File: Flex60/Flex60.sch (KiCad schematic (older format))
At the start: 112 parts

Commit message: Layout Diodes + add flex cuts
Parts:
- removed D31: BAV70, Custom_Footprints:SOT-23_Annotated, symbol Diode:BAV70
- renumbered D32 to D31, D33 to D32
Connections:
- net at K_0.2: now also D1.2 (A); no longer D1.1 (A)
- net at K_1.2: now also D1.1 (A); no longer D1.2 (A)
- net at K_100.2: now also D8.2 (A); no longer D8.1 (A)
- net at K_101.2: now also D8.1 (A); no longer D8.2 (A)
- net at K_200.2, K_200A1.2: now also D15.2 (A); no longer D15.1 (A)
- net at K_201.2: now also D15.1 (A); no longer D15.2 (A)
- net at K_300.2: now also D22.2 (A); no longer D22.1 (A)
- net at K_301.2: now also D22.1 (A); no longer D22.2 (A)
- net at K_400.2, K_400A1.2: now also D29.2 (A); no longer D29.1 (A)
- net at K_401.2, K_401A1.2: now also D29.1 (A); no longer D29.2 (A)
- net at K_2.2: now also D2.2 (A); no longer D2.1 (A)
- net at K_3.2: now also D2.1 (A); no longer D2.2 (A)
- net at K_102.2: now also D9.2 (A); no longer D9.1 (A)
- net at K_103.2: now also D9.1 (A); no longer D9.2 (A)
- net at K_202.2: now also D16.2 (A); no longer D16.1 (A)
- net at K_203.2: now also D16.1 (A); no longer D16.2 (A)
- net at K_302.2: now also D23.2 (A); no longer D23.1 (A)
- net at K_303.2: now also D23.1 (A); no longer D23.2 (A)
- net at K_402.2, K_402A1.2: now also D30.2 (A); no longer D30.1 (A)
- net at K_4.2: now also D3.2 (A); no longer D3.1 (A)
- net at K_5.2: now also D3.1 (A); no longer D3.2 (A)
- net at K_104.2: now also D10.2 (A); no longer D10.1 (A)
- net at K_105.2: now also D10.1 (A); no longer D10.2 (A)
- net at K_204.2: now also D17.2 (A); no longer D17.1 (A)
- net at K_205.2: now also D17.1 (A); no longer D17.2 (A)
- net at K_304.2: now also D24.2 (A); no longer D24.1 (A)
- net at K_305.2: now also D24.1 (A); no longer D24.2 (A)
- net at K_6.2: now also D4.2 (A); no longer D4.1 (A)
- net at K_7.2: now also D4.1 (A); no longer D4.2 (A)
- net at K_106.2: now also D11.2 (A); no longer D11.1 (A)
- net at K_107.2: now also D11.1 (A); no longer D11.2 (A)
- net at K_206.2: now also D18.2 (A); no longer D18.1 (A)
- net at K_207.2: now also D18.1 (A); no longer D18.2 (A)
- net at K_306.2: now also D25.2 (A); no longer D25.1 (A)
- net at K_307.2: now also D25.1 (A); no longer D25.2 (A)
- net at K_406.2, K_406A1.2: now also D30.1 (A)
- net at K_8.2: now also D5.2 (A); no longer D5.1 (A)
- net at K_9.2: now also D5.1 (A); no longer D5.2 (A)
- net at K_108.2: now also D12.2 (A); no longer D12.1 (A)
- net at K_109.2: now also D12.1 (A); no longer D12.2 (A)
- net at K_208.2: now also D19.2 (A); no longer D19.1 (A)
- net at K_209.2: now also D19.1 (A); no longer D19.2 (A)
- net at K_308.2: now also D26.2 (A); no longer D26.1 (A)
- net at K_309.2: now also D26.1 (A); no longer D26.2 (A)
- net at K_408.2: now also D31.2 (A); no longer D31.1 (A)
- net at K_409.2, K_409A1.2: now also D31.1 (A); no longer D31.2 (A)
- net at K_10.2: now also D6.2 (A); no longer D6.1 (A)
- net at K_11.2: now also D6.1 (A); no longer D6.2 (A)
- net at K_110.2: now also D13.2 (A); no longer D13.1 (A)
- net at K_111.2: now also D13.1 (A); no longer D13.2 (A)
- net at K_210.2: now also D20.2 (A); no longer D20.1 (A)
- net at K_211.2: now also D20.1 (A); no longer D20.2 (A)
- net at K_310.2: now also D27.2 (A); no longer D27.1 (A)
- net at K_311.2, K_311A1.2: now also D27.1 (A); no longer D27.2 (A)
- net at K_410.2, K_410A1.2: now also D32.2 (A); no longer D32.1 (A)
- net at K_411.2, K_411A1.2: now also D32.1 (A); no longer D32.2 (A)
- net at K_12.2: now also D7.2 (A); no longer D7.1 (A)
- net at K_013A1.2, K_13.2: now also D7.1 (A); no longer D7.2 (A)
- net at K_112.2: now also D14.2 (A); no longer D14.1 (A)
- net at K_113.2: now also D14.1 (A); no longer D14.2 (A)
- net at K_212.2: now also D21.2 (A); no longer D21.1 (A)
- net at K_213.2: now also D21.1 (A); no longer D21.2 (A)
- no-connect marks 3 -> 1
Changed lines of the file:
@@
 F 3 "https://assets.nexperia.com/documents/data-sheet/BAV70_SER.pdf" H 1275 875 50  0001 C CNN
 	1    1275 875
-	1    0    0    -1
+	-1   0    0    -1
 $EndComp
 $Comp
@@
 F 3 "https://assets.nexperia.com/documents/data-sheet/BAV70_SER.pdf" H 1275 1450 50  0001 C CNN
 	1    1275 1450
-	1    0    0    -1
+	-1   0    0    -1
 $EndComp
 $Comp
@@
 F 3 "https://assets.nexperia.com/documents/data-sheet/BAV70_SER.pdf" H 1275 2025 50  0001 C CNN
 	1    1275 2025
-	1    0    0    -1
+	-1   0    0    -1
 $EndComp
 $Comp
@@
 F 3 "https://assets.nexperia.com/documents/data-sheet/BAV70_SER.pdf" H 1275 2600 50  0001 C CNN
 	1    1275 2600
-	1    0    0    -1
+	-1   0    0    -1
 $EndComp
 $Comp
@@
 F 3 "https://assets.nexperia.com/documents/data-sheet/BAV70_SER.pdf" H 1275 3175 50  0001 C CNN
 	1    1275 3175
-	1    0    0    -1
+	-1   0    0    -1
 $EndComp
 $Comp
@@
 F 3 "https://assets.nexperia.com/documents/data-sheet/BAV70_SER.pdf" H 2800 875 50  0001 C CNN
 	1    2800 875
-	1    0    0    -1
+	-1   0    0    -1
 $EndComp
 $Comp
@@
 F 3 "https://assets.nexperia.com/documents/data-sheet/BAV70_SER.pdf" H 2800 1450 50  0001 C CNN
 	1    2800 1450
-	1    0    0    -1
+	-1   0    0    -1
 $EndComp
 $Comp
@@
 F 3 "https://assets.nexperia.com/documents/data-sheet/BAV70_SER.pdf" H 2800 2025 50  0001 C CNN
 	1    2800 2025
-	1    0    0    -1
+	-1   0    0    -1
 $EndComp
 $Comp
@@
 F 3 "https://assets.nexperia.com/documents/data-sheet/BAV70_SER.pdf" H 2800 2600 50  0001 C CNN
 	1    2800 2600
-	1    0    0    -1
+	-1   0    0    -1
 $EndComp
 $Comp
@@
 F 3 "https://assets.nexperia.com/documents/data-sheet/BAV70_SER.pdf" H 2800 3175 50  0001 C CNN
 	1    2800 3175
-	1    0    0    -1
+	-1   0    0    -1
 $EndComp
 Wire Wire Line
@@
 F 3 "https://assets.nexperia.com/documents/data-sheet/BAV70_SER.pdf" H 4325 875 50  0001 C CNN
 	1    4325 875
-	1    0    0    -1
+	-1   0    0    -1
 $EndComp
 $Comp
@@
 F 3 "https://assets.nexperia.com/documents/data-sheet/BAV70_SER.pdf" H 4325 1450 50  0001 C CNN
 	1    4325 1450
-	1    0    0    -1
+	-1   0    0    -1
 $EndComp
 $Comp
@@
 F 3 "https://assets.nexperia.com/documents/data-sheet/BAV70_SER.pdf" H 4325 2025 50  0001 C CNN
 	1    4325 2025
-	1    0    0    -1
+	-1   0    0    -1
 $EndComp
 $Comp
@@
 F 3 "https://assets.nexperia.com/documents/data-sheet/BAV70_SER.pdf" H 4325 2600 50  0001 C CNN
 	1    4325 2600
-	1    0    0    -1
+	-1   0    0    -1
 $EndComp
 Wire Wire Line
@@
 F 3 "https://assets.nexperia.com/documents/data-sheet/BAV70_SER.pdf" H 5850 875 50  0001 C CNN
 	1    5850 875
-	1    0    0    -1
+	-1   0    0    -1
 $EndComp
 $Comp
@@
 F 3 "https://assets.nexperia.com/documents/data-sheet/BAV70_SER.pdf" H 5850 1450 50  0001 C CNN
 	1    5850 1450
-	1    0    0    -1
+	-1   0    0    -1
 $EndComp
 $Comp
@@
 F 3 "https://assets.nexperia.com/documents/data-sheet/BAV70_SER.pdf" H 5850 2025 50  0001 C CNN
 	1    5850 2025
-	1    0    0    -1
+	-1   0    0    -1
 $EndComp
 $Comp
@@
 F 3 "https://assets.nexperia.com/documents/data-sheet/BAV70_SER.pdf" H 5850 2600 50  0001 C CNN
 	1    5850 2600
-	1    0    0    -1
+	-1   0    0    -1
 $EndComp
 $Comp
@@
 	1    0    0    -1
 $EndComp
-$Comp
-L Diode:BAV70 D31
-U 1 1 5FD7F567
-P 5850 3175
-F 0 "D31" H 5850 3392 50  0000 C CNN
-F 1 "BAV70" H 5850 3301 50  0000 C CNN
-F 2 "Custom_Footprints:SOT-23_Annotated" H 5850 3175 50  0001 C CNN
-F 3 "https://assets.nexperia.com/documents/data-sheet/BAV70_SER.pdf" H 5850 3175 50  0001 C CNN
-	1    5850 3175
-	1    0    0    -1
-$EndComp
 Wire Wire Line
 	5850 2225 4325 2225
@@
 F 3 "https://assets.nexperia.com/documents/data-sheet/BAV70_SER.pdf" H 7375 875 50  0001 C CNN
 	1    7375 875
-	1    0    0    -1
+	-1   0    0    -1
 $EndComp
 $Comp
@@
 F 3 "https://assets.nexperia.com/documents/data-sheet/BAV70_SER.pdf" H 7375 1450 50  0001 C CNN
 	1    7375 1450
-	1    0    0    -1
+	-1   0    0    -1
 $EndComp
 $Comp
@@
 F 3 "https://assets.nexperia.com/documents/data-sheet/BAV70_SER.pdf" H 7375 2025 50  0001 C CNN
 	1    7375 2025
-	1    0    0    -1
+	-1   0    0    -1
 $EndComp
 $Comp
@@
 F 3 "https://assets.nexperia.com/documents/data-sheet/BAV70_SER.pdf" H 7375 2600 50  0001 C CNN
 	1    7375 2600
-	1    0    0    -1
+	-1   0    0    -1
 $EndComp
 $Comp
@@
 $EndComp
 $Comp
-L Diode:BAV70 D32
+L Diode:BAV70 D31
 U 1 1 5FD83E49
 P 7375 3175
-F 0 "D32" H 7375 3392 50  0000 C CNN
+F 0 "D31" H 7375 3392 50  0000 C CNN
 F 1 "BAV70" H 7375 3301 50  0000 C CNN
 F 2 "Custom_Footprints:SOT-23_Annotated" H 7375 3175 50  0001 C CNN
 F 3 "https://assets.nexperia.com/documents/data-sheet/BAV70_SER.pdf" H 7375 3175 50  0001 C CNN
 	1    7375 3175
-	1    0    0    -1
+	-1   0    0    -1
 $EndComp
 Wire Wire Line
@@
 Wire Wire Line
 	7375 2800 5850 2800
-Wire Wire Line
-	7375 3375 5850 3375
 Wire Wire Line
 	7375 1650 5850 1650
@@
 F 3 "https://assets.nexperia.com/documents/data-sheet/BAV70_SER.pdf" H 8900 875 50  0001 C CNN
 	1    8900 875
-	1    0    0    -1
+	-1   0    0    -1
 $EndComp
 $Comp
@@
 F 3 "https://assets.nexperia.com/documents/data-sheet/BAV70_SER.pdf" H 8900 1450 50  0001 C CNN
 	1    8900 1450
-	1    0    0    -1
+	-1   0    0    -1
 $EndComp
 $Comp
@@
 F 3 "https://assets.nexperia.com/documents/data-sheet/BAV70_SER.pdf" H 8900 2025 50  0001 C CNN
 	1    8900 2025
-	1    0    0    -1
+	-1   0    0    -1
 $EndComp
 $Comp
@@
 F 3 "https://assets.nexperia.com/documents/data-sheet/BAV70_SER.pdf" H 8900 2600 50  0001 C CNN
 	1    8900 2600
-	1    0    0    -1
+	-1   0    0    -1
 $EndComp
 $Comp
@@
 $EndComp
 $Comp
-L Diode:BAV70 D33
+L Diode:BAV70 D32
 U 1 1 5FD882CA
 P 8900 3175
-F 0 "D33" H 8900 3392 50  0000 C CNN
+F 0 "D32" H 8900 3392 50  0000 C CNN
 F 1 "BAV70" H 8900 3301 50  0000 C CNN
 F 2 "Custom_Footprints:SOT-23_Annotated" H 8900 3175 50  0001 C CNN
 F 3 "https://assets.nexperia.com/documents/data-sheet/BAV70_SER.pdf" H 8900 3175 50  0001 C CNN
 	1    8900 3175
-	1    0    0    -1
+	-1   0    0    -1
 $EndComp
 Wire Wire Line
@@
 F 3 "https://assets.nexperia.com/documents/data-sheet/BAV70_SER.pdf" H 10425 875 50  0001 C CNN
 	1    10425 875
-	1    0    0    -1
+	-1   0    0    -1
 $EndComp
 $Comp
@@
 F 3 "https://assets.nexperia.com/documents/data-sheet/BAV70_SER.pdf" H 10425 1450 50  0001 C CNN
 	1    10425 1450
-	1    0    0    -1
+	-1   0    0    -1
 $EndComp
 $Comp
@@
 F 3 "https://assets.nexperia.com/documents/data-sheet/BAV70_SER.pdf" H 10425 2025 50  0001 C CNN
 	1    10425 2025
-	1    0    0    -1
+	-1   0    0    -1
 $EndComp
 $Comp
@@
 Text GLabel 11125 875  1    50   Input ~ 0
 col13
-Wire Wire Line
-	2800 3375 5850 3375
 NoConn ~ 10725 2600
-NoConn ~ 6150 3175
-NoConn ~ 3100 3175
 $Comp
 L Switch:SW_Push K_400A1
@@
 Wire Wire Line
 	5550 3225 5550 3175
-Connection ~ 5550 3175
 Wire Wire Line
 	8200 3225 8200 3175
@@
 	7675 3225 7675 3175
 Connection ~ 7675 3175
+Connection ~ 2800 1075
+Connection ~ 4325 1075
+Connection ~ 5850 1075
+Connection ~ 7375 1075
+Connection ~ 8900 1075
+Connection ~ 8900 1650
+Connection ~ 7375 1650
+Connection ~ 5850 1650
+Connection ~ 4325 1650
+Connection ~ 2800 1650
+Connection ~ 2800 2225
+Connection ~ 4325 2225
+Connection ~ 5850 2225
+Connection ~ 7375 2225
+Connection ~ 8900 2225
+Connection ~ 8900 2800
+Connection ~ 7375 2800
+Connection ~ 5850 2800
+Connection ~ 4325 2800
+Connection ~ 2800 2800
+Connection ~ 2800 3375
+Connection ~ 7375 3375
+Wire Wire Line
+	2800 3375 7375 3375
+Wire Wire Line
+	5550 3175 5650 3175
+Wire Wire Line
+	5650 3175 5650 3300
+Wire Wire Line
+	5650 3300 3100 3300
+Wire Wire Line
+	3100 3300 3100 3175
+Connection ~ 5550 3175
 $EndSCHEMATC

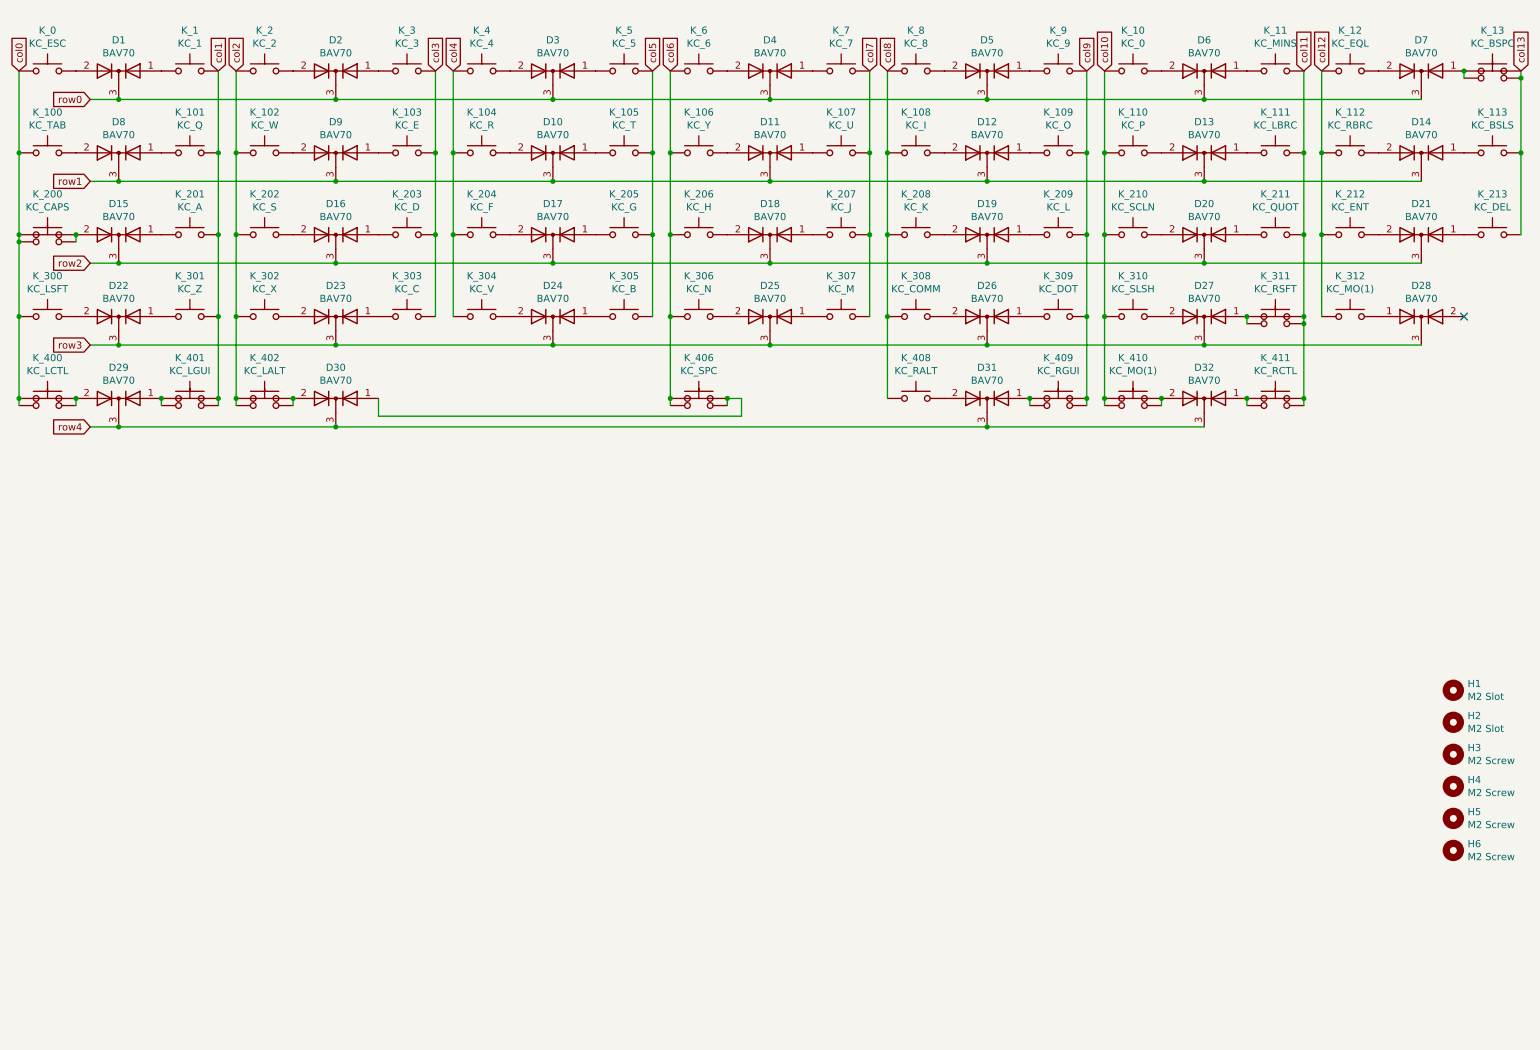
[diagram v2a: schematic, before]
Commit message: Add MCU + USB circuits
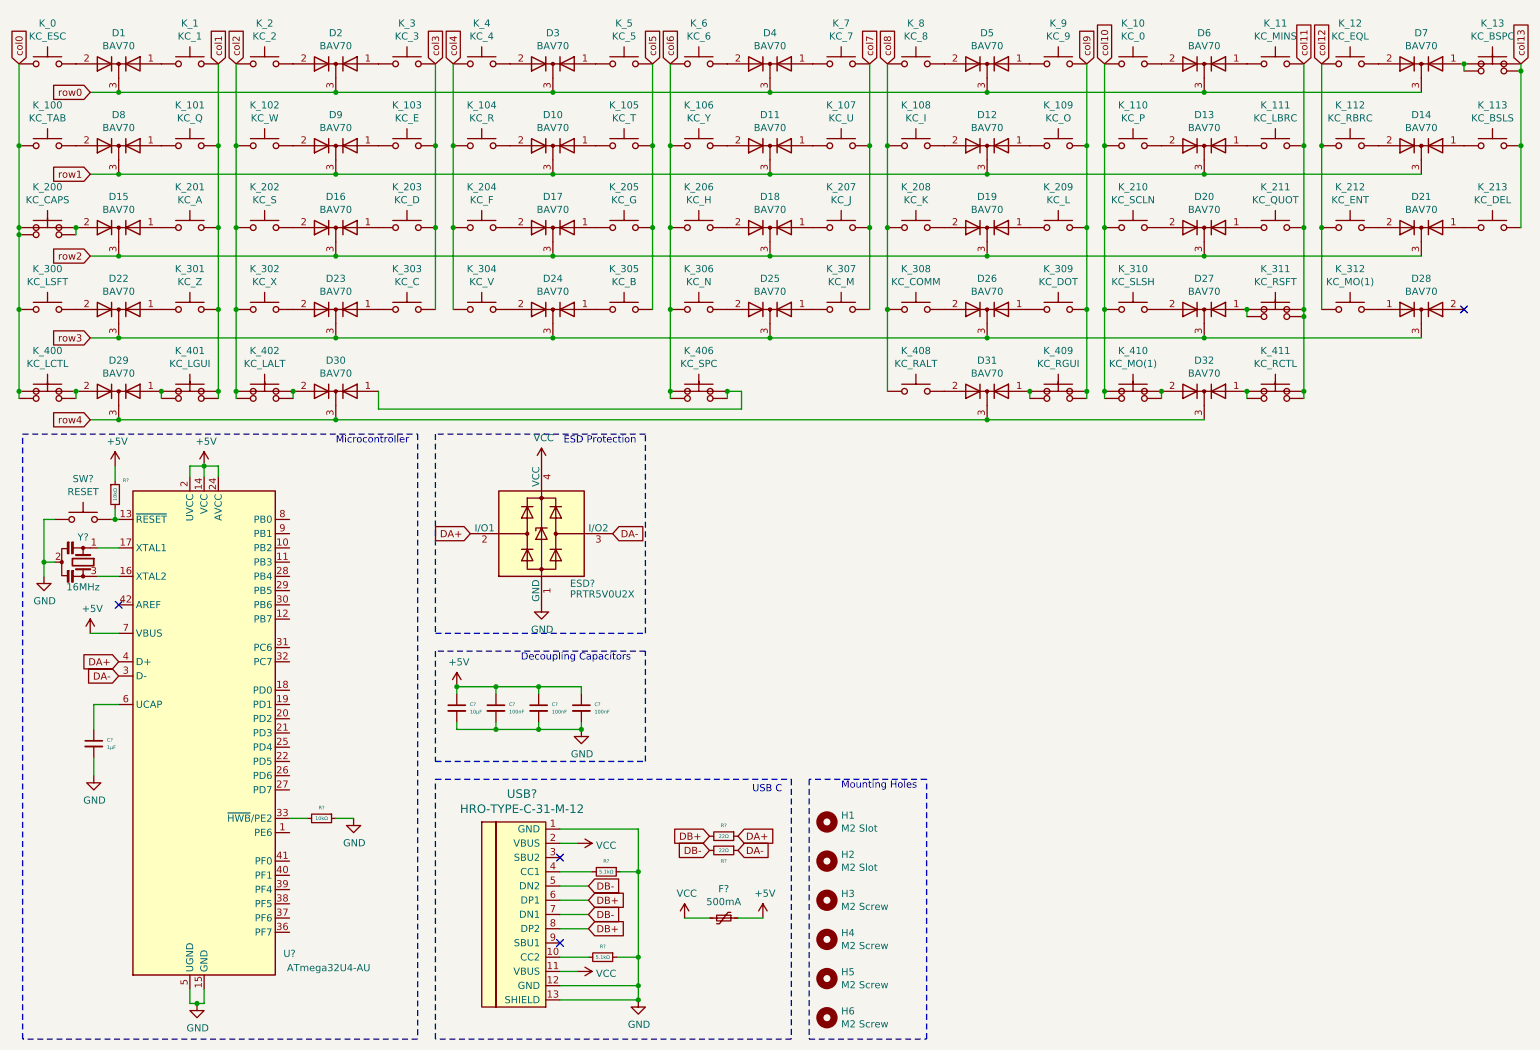
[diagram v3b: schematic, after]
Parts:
- added C?: 1µF, symbol Device:C_Small
- added C?: 10µF, symbol Device:C_Small
- added C? (x3): 100nF, symbol Device:C_Small
- added ESD?: PRTR5V0U2X, Package_TO_SOT_SMD:SOT-143, symbol Power_Protection:PRTR5V0U2X
- added F?: 500mA, symbol Device:Polyfuse_Small
- added R? (x2): 5.1kΩ, symbol Device:R_Small
- added R? (x2): 22Ω, symbol Device:R_Small
- added R? (x2): 10kΩ, symbol Device:R_Small
- added SW?: RESET, symbol Switch:SW_Push
- added U?: ATmega32U4-AU, Package_QFP:TQFP-44_10x10mm_P0.8mm, symbol MCU_Microchip_ATmega:ATmega32U4-AU
- added USB?: HRO-TYPE-C-31-M-12, symbol Type-C:HRO-TYPE-C-31-M-12
- added Y?: 16MHz, symbol Device:Resonator_Small
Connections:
- new net: R?.2, USB?.10 (CC2)
- new net: R?.2, USB?.4 (CC1)
- new net: R?.2, SW?.2, U?.13 (~RESET)
- new net: U?.16 (XTAL2), Y?.3
- new net: U?.17 (XTAL1), Y?.1
- new net: R?.2, U?.33 (~HWB~/PE2)
- new net: C?.1, U?.6 (UCAP)
- new net +5V: C?.1, C?.1, C?.1, C?.1, F?.1, R?.1, U?.14 (VCC), U?.2 (UVCC), U?.24 (AVCC), U?.34 (VCC), U?.44 (AVCC), U?.7 (VBUS)
- new net DA+: ESD?.2 (I/O1), R?.1, U?.4 (D+)
- new net DA-: ESD?.3 (I/O2), R?.1, U?.3 (D-)
- new net DB+: R?.2, USB?.6 (DP1), USB?.8 (DP2)
- new net DB-: R?.2, USB?.5 (DN2), USB?.7 (DN1)
- new net GND: C?.2, C?.2, C?.2, C?.2, C?.2, ESD?.1 (GND), R?.1, R?.1, R?.1, SW?.1, U?.15 (GND), U?.23 (GND), U?.35 (GND), U?.43 (GND), U?.5 (UGND), USB?.1 (GND), USB?.12 (GND), USB?.13 (SHIELD), Y?.2
- new net VCC: ESD?.4 (VCC), F?.2, USB?.11 (VBUS), USB?.2 (VBUS)
- no-connect marks 1 -> 4
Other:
- note added: "Decoupling Capacitors"
- note added: "ESD Protection"
- note added: "Microcontroller"
- note added: "Mounting Holes"
- note added: "USB C"
- moved on the sheet: D1, D10, D11, D12, D13, D14, D15, D16, D17, D18, D19, D2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

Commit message: Add Footprints + 3D models
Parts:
- C1, C2, C3, C4, C5: renamed from C?; footprint (none) -> Custom_Footprints:C_0603_Annotated
- F1: renamed from F?; footprint (none) -> Custom_Footprints:Fuse_1206_Annotated
- R1, R2, R3, R4, R5, R6: renamed from R?; footprint (none) -> Custom_Footprints:R_0603_Annotated
- SW1: renamed from SW?; footprint (none) -> Custom_Footprints:Tactile_Switch
- U1: renamed from U?; footprint Package_QFP:TQFP-44_10x10mm_P0.8mm -> Custom_Footprints:ATMEGA32U4_Annotated
- USB1: renamed from USB?; footprint (none) -> Type-C:HRO-TYPE-C-31-M-12
- Y1: renamed from Y?; footprint (none) -> Custom_Footprints:Resonator_3Pin_Annotated
- gave numbers to parts that had none: 1
